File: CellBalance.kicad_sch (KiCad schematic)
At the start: 9 parts

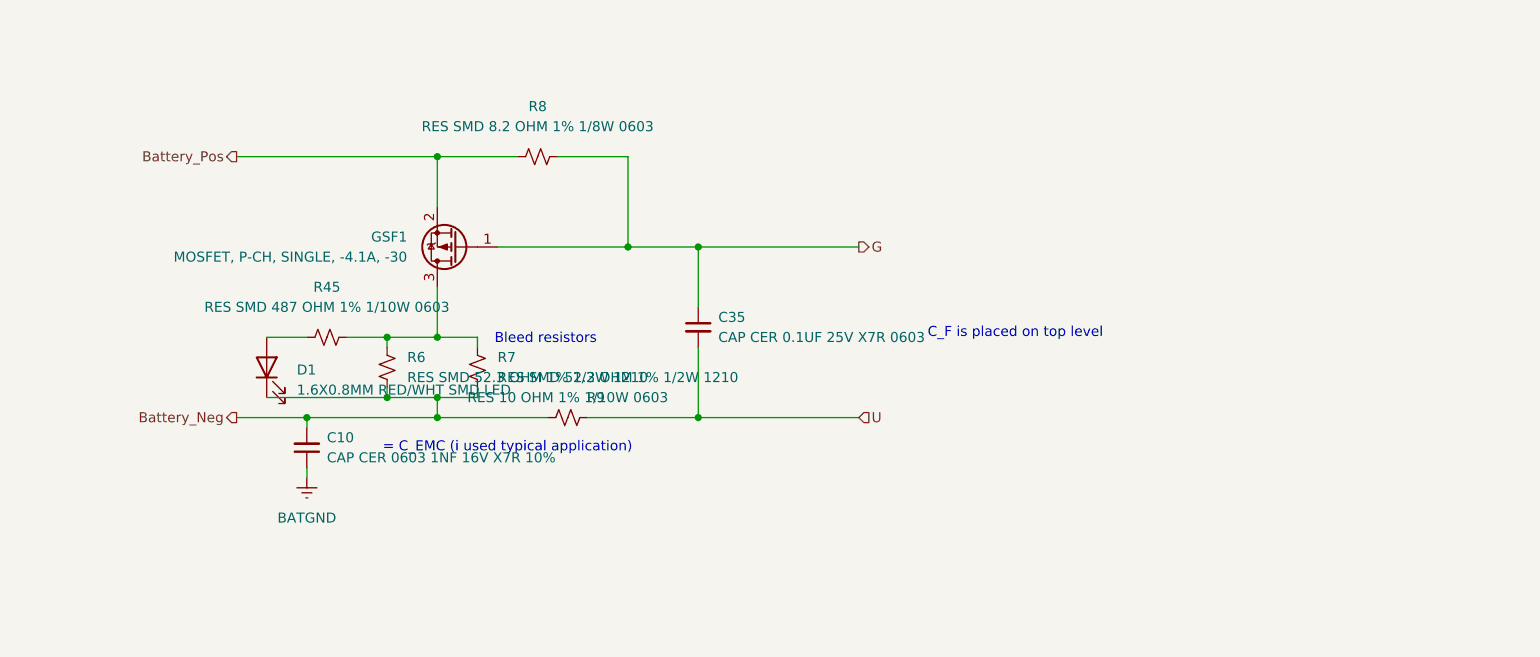
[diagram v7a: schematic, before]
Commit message: cleaned up schematic
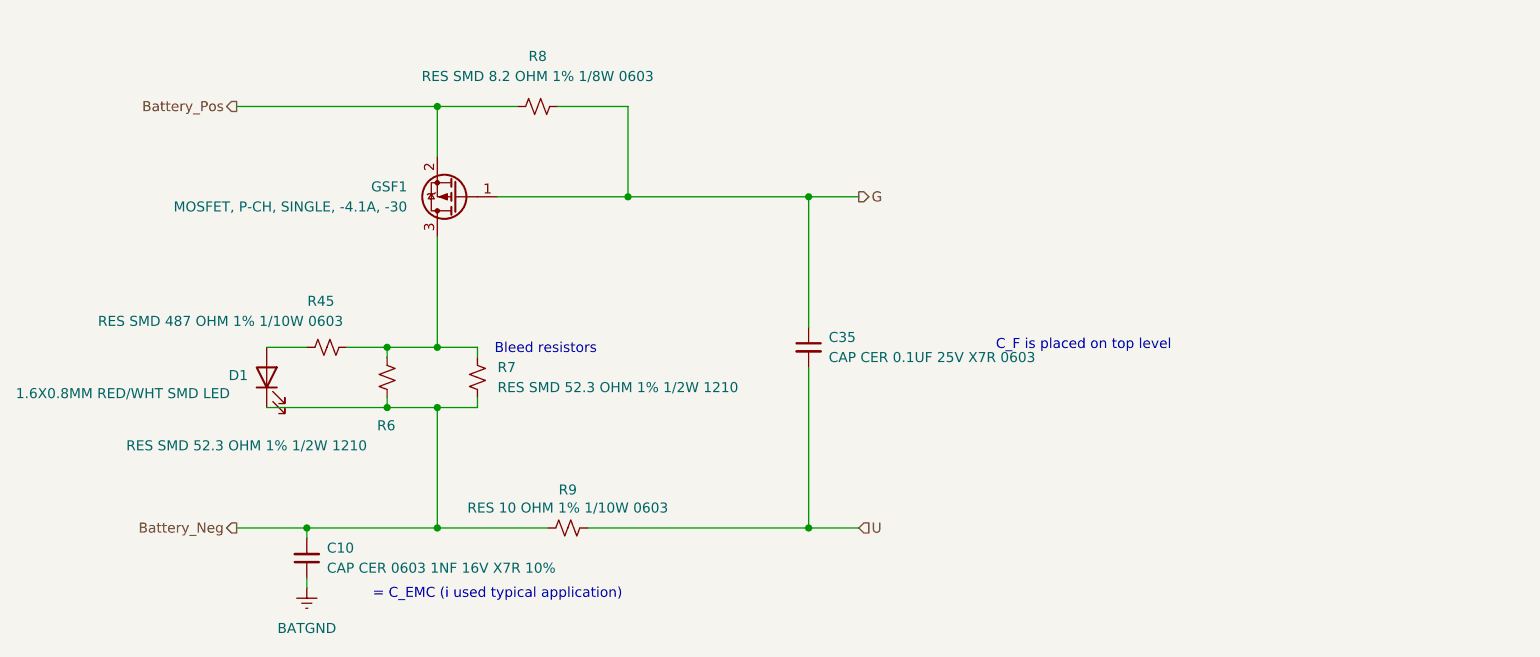
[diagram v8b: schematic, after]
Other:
- moved on the sheet: C10, C35, D1, GSF1, R45, R6, R7, R8, R9
